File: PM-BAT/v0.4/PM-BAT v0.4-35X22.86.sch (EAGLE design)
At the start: 87 parts, among them J1 M13PTH-CST-R, J2 M12PTH-CST-R, U1 BQ24195, U2 TPS63020, U3 TPS631011, U5 TPS22918, U6 SPARKFUN-POWERIC_MAX1704X

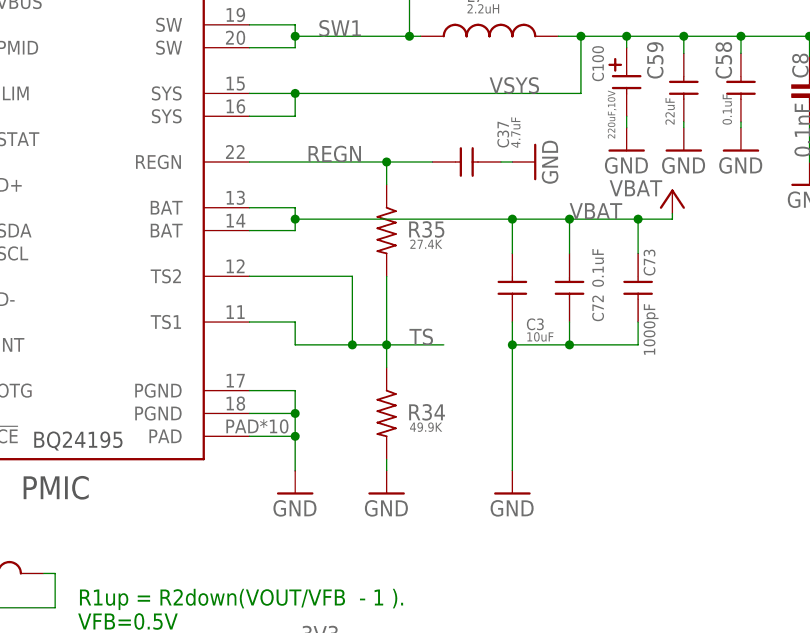
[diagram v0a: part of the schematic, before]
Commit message: update
add shield case DXF
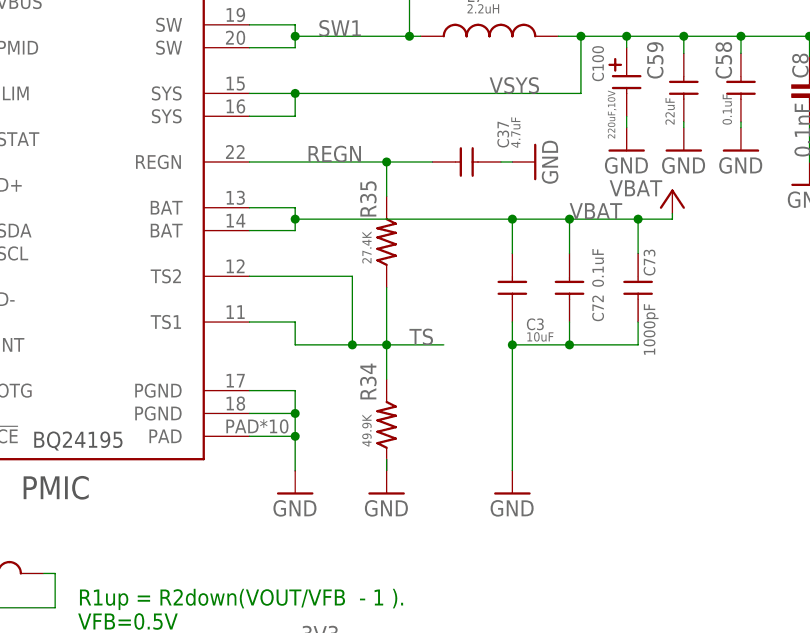
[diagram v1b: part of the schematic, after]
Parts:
- R34, R35: device Spark:R-US_ -> particle SZ:RESR0201-N
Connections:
- net GND: now also R34.1; no longer R34.2
- net REGN: now also R35.2; no longer R35.1
- net TS: now also R34.2, R35.1; no longer R34.1, R35.2
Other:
- moved on the sheet: R34, R35

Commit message: update
output gerber for MO DFM
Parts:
- C12: device particle SZ:RESR0603A -> particle SZ:CAPC0603
- L1, L3: value 2.2uH -> 1.5uH
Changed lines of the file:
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@@
 <attribute name="ITEM_NUMBER" value="PT-200695"/>
-</part>
-<part name="C12" library="particle SZ" deviceset="RES" device="R0603A" value="22uF 10V">
-<attribute name="ITEM_NAME" value="CAP CER 0.1UF 16V X7R 0402 10%"/>
-<attribute name="ITEM_NUMBER" value="120-00060"/>
 </part>
 <part name="GND6" library="supply1" deviceset="GND" device=""/>
@@
 <attribute name="ITEM_NUMBER" value="PT-200138"/>
 </part>
-<part name="L1" library="Particle" deviceset="INDUCTOR-SPARKFUN" device="INDUCTOR-2520" value="2.2uH">
+<part name="L1" library="Particle" deviceset="INDUCTOR-SPARKFUN" device="INDUCTOR-2520" value="1.5uH">
 <attribute name="ITEM_NAME" value=""/>
 <attribute name="ITEM_NUMBER" value=""/>
@@
 <attribute name="ITEM_NUMBER" value="PT-200138"/>
 </part>
-<part name="L3" library="Particle" deviceset="INDUCTOR-SPARKFUN" device="INDUCTOR-2520" value="2.2uH">
+<part name="L3" library="Particle" deviceset="INDUCTOR-SPARKFUN" device="INDUCTOR-2520" value="1.5uH">
 <attribute name="ITEM_NAME" value=""/>
 <attribute name="ITEM_NUMBER" value=""/>
@@
 <attribute name="ITEM_NUMBER" value=""/>
 </part>
+<part name="C12" library="particle SZ" library_urn="urn:adsk.eagle:library:21650216" deviceset="CAP" device="C0603" package3d_urn="urn:adsk.eagle:package:21650777/5" value="22uF 10V">
+<attribute name="ITEM_NAME" value="CAP CER 0.1UF 16V X7R 0402 10%"/>
+<attribute name="ITEM_NUMBER" value="120-00060"/>
+</part>
 </parts>
 <sheets>
@@
 <attribute name="ITEM_NAME" x="244.475" y="99.06" size="1.778" layer="96" display="off"/>
 </instance>
-<instance part="C12" gate="G$1" x="58.42" y="24.13" smashed="yes" rot="R270">
-<attribute name="NAME" x="57.15" y="28.575" size="1.27" layer="95" rot="R90"/>
-<attribute name="VALUE" x="57.15" y="15.875" size="1.27" layer="96" rot="R90"/>
-<attribute name="ITEM_NUMBER" x="58.42" y="24.13" size="1.778" layer="96" rot="R270" display="off"/>
-<attribute name="ITEM_NAME" x="58.42" y="24.13" size="1.778" layer="96" rot="R270" display="off"/>
-</instance>
 <instance part="GND6" gate="1" x="58.42" y="1.27" smashed="yes">
 <attribute name="VALUE" x="55.88" y="-1.27" size="1.778" layer="96"/>
@@
 <attribute name="VALUE" x="160.8836" y="63.5762" size="1.016" layer="96" rot="R90"/>
 <attribute name="ITEM_NUMBER" x="162.56" y="66.04" size="1.778" layer="96" rot="R90" display="off"/>
+</instance>
+<instance part="C12" gate="G$1" x="58.42" y="22.86" smashed="yes">
+<attribute name="NAME" x="57.15" y="26.035" size="1.27" layer="95" rot="R90"/>
+<attribute name="VALUE" x="57.15" y="14.605" size="1.27" layer="96" rot="R90"/>
+<attribute name="ITEM_NUMBER" x="58.42" y="22.86" size="1.778" layer="96" display="off"/>
+<attribute name="ITEM_NAME" x="58.42" y="22.86" size="1.778" layer="96" display="off"/>
 </instance>
 </instances>
@@
 <segment>
 <pinref part="GND6" gate="1" pin="GND"/>
-<pinref part="C12" gate="G$1" pin="2"/>
 <wire x1="58.42" y1="13.97" x2="58.42" y2="3.81" width="0.1524" layer="91"/>
-<wire x1="58.42" y1="19.05" x2="58.42" y2="13.97" width="0.1524" layer="91"/>
 <wire x1="63.5" y1="13.97" x2="58.42" y2="13.97" width="0.1524" layer="91"/>
 <junction x="58.42" y="13.97"/>
 <pinref part="C13" gate="G$1" pin="2"/>
 <wire x1="63.5" y1="13.97" x2="63.5" y2="20.32" width="0.1524" layer="91"/>
+<pinref part="C12" gate="G$1" pin="2"/>
+<wire x1="58.42" y1="20.32" x2="58.42" y2="13.97" width="0.1524" layer="91"/>
 </segment>
 <segment>
@@
 <wire x1="63.5" y1="34.29" x2="58.42" y2="34.29" width="0.1524" layer="91"/>
 <label x="56.4642" y="34.8996" size="1.778" layer="95"/>
-<pinref part="C12" gate="G$1" pin="1"/>
-<wire x1="58.42" y1="29.21" x2="58.42" y2="34.29" width="0.1524" layer="91"/>
 <junction x="63.5" y="34.29"/>
 <pinref part="R14" gate="G$1" pin="1"/>
@@
 <wire x1="86.36" y1="33.401" x2="86.36" y2="34.29" width="0.1524" layer="91"/>
 <junction x="86.36" y="34.29"/>
+<pinref part="C12" gate="G$1" pin="1"/>
+<wire x1="58.42" y1="27.94" x2="58.42" y2="34.29" width="0.1524" layer="91"/>
 </segment>
 <segment>
@@
 </nets>
 </sheet>
+<sheet>
+<plain>
+</plain>
+<instances>
+</instances>
+<busses>
+</busses>
+<nets>
+</nets>
+</sheet>
